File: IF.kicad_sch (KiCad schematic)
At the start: 34 parts, among them J1 JACK_TRS_3pins, U16 NE5532

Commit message: schematics mixer progress, 74HC4053, IF RX. PCB update
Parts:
- removed C16, C17: 220pF, LCSDR:C_Disc_D7.5mm_W2.5mm_P5.00mm, symbol C_Small
- removed C18, C6: 100nF, LCSDR:C_1206_0603, symbol C_Small
- removed C19, C33, C45: 10uF, LCSDR:CP_Radial_D5.0mm_P2.00mm, symbol CP_Small
- removed C25, C4, C5, C8: 27nF, LCSDR:C_1206_0603, symbol C_Small
- removed C32, C35, C62, C63: 10uF, Capacitors_THT:CP_Radial_D5.0mm_P2.00mm, symbol CP_Small
- removed J1: JACK_TRS_3pins, LCSDR:audio_jack_3_5mm_PJ307, symbol JACK_TRS_3pins
- removed L3: 100uH, Resistors_THT:R_Axial_DIN0207_L6.3mm_D2.5mm_P15.24mm_Horizontal, symbol L_Small
- removed R14, R17, R24, R46: 1k, LCSDR:R_0603_HandSoldering, symbol R_Small
- removed R2, R3, R32, R33: 33R, LCSDR:R_1206_0603, symbol R_Small
- removed R47, R48, R49, R50: 22k, LCSDR:R_0603_HandSoldering, symbol R_Small
- removed R51, R62: 1k, LCSDR:R_1206_0603, symbol R_Small
- removed R63, R64: 10k, LCSDR:R_0603_HandSoldering, symbol R_Small
- removed U16: NE5532, Housings_SOIC:SOIC-8_3.9x4.9mm_Pitch1.27mm, symbol NE5532
- added K1: G5V-2_Split, Relay_THT:Relay_DPDT_Omron_G5V-2, symbol Relay:G5V-2_Split
- added R8: 3k, symbol Device:R_Small
- added U5: MC33079, symbol Amplifier_Operational:MC33079

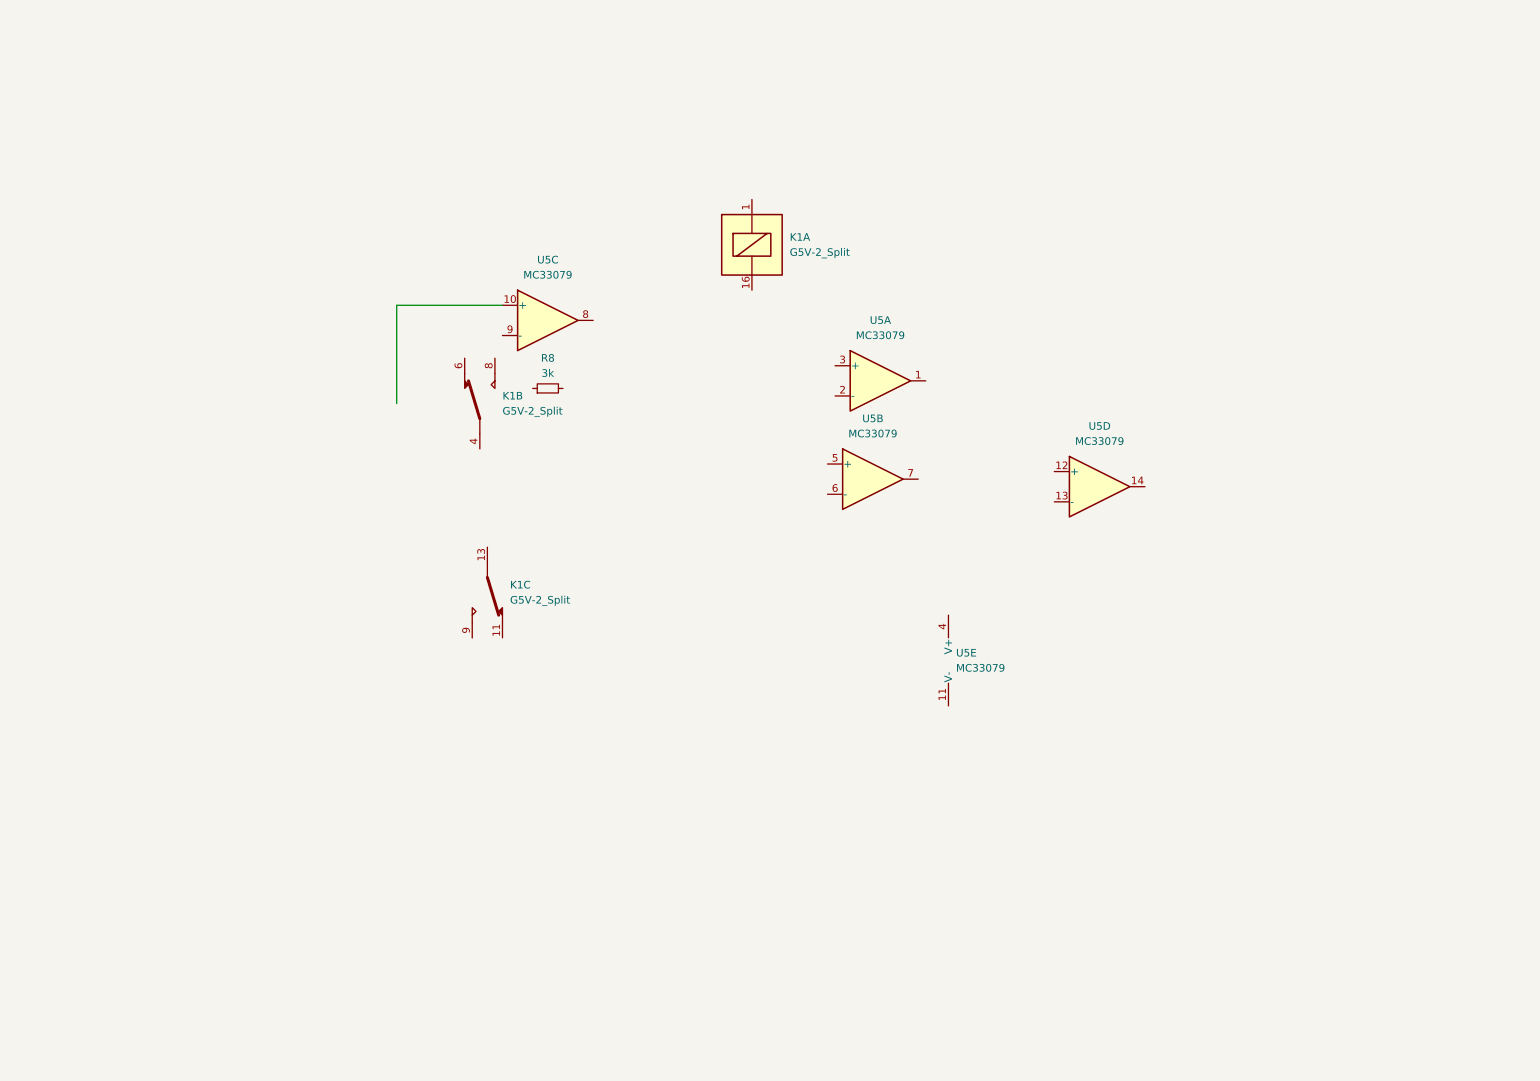
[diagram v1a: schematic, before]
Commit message: schematics mixer, 74HC4053. IF RX needs JLCPCB numbers. PCB update
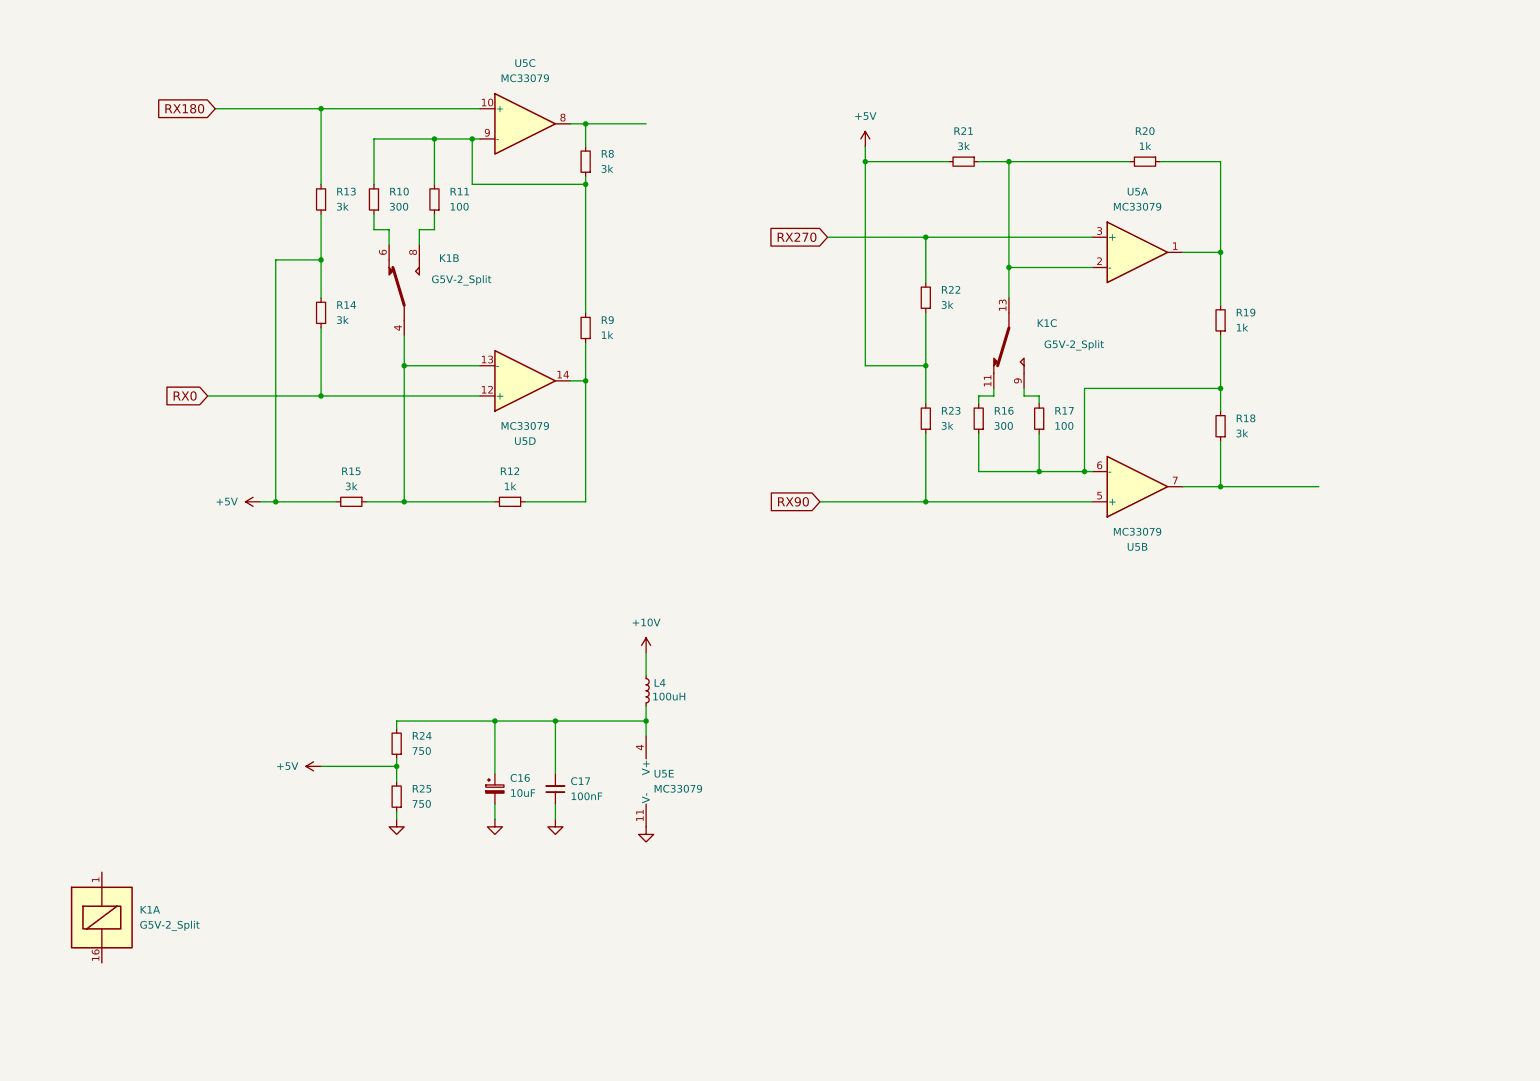
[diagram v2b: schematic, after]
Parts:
- added C16: 10uF, Capacitor_Tantalum_SMD:CP_EIA-3216-18_Kemet-A_Pad1.58x1.35mm_HandSolder, symbol Device:C_Polarized_Small
- added C17: 100nF, Capacitor_SMD:C_0603_1608Metric_Pad1.08x0.95mm_HandSolder, symbol Device:C_Small
- added L4: 100uH, Inductor_SMD:L_1210_3225Metric_Pad1.42x2.65mm_HandSolder, symbol Device:L_Small
- added R10, R16: 300, Resistor_SMD:R_0603_1608Metric_Pad0.98x0.95mm_HandSolder, symbol Device:R_Small
- added R11, R17: 100, Resistor_SMD:R_0603_1608Metric_Pad0.98x0.95mm_HandSolder, symbol Device:R_Small
- added R12, R19, R20, R9: 1k, Resistor_SMD:R_0603_1608Metric_Pad0.98x0.95mm_HandSolder, symbol Device:R_Small
- added R13, R14, R15, R18, R21, R22, R23: 3k, Resistor_SMD:R_0603_1608Metric_Pad0.98x0.95mm_HandSolder, symbol Device:R_Small
- added R24, R25: 750, Resistor_SMD:R_0603_1608Metric_Pad0.98x0.95mm_HandSolder, symbol Device:R_Small
- R8: footprint (none) -> Resistor_SMD:R_0603_1608Metric_Pad0.98x0.95mm_HandSolder
- U5: footprint (none) -> Package_SO:SOIC-14_3.9x8.7mm_P1.27mm
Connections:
- net RX180: now reaches U5.10 (+)
- net RX180: now also R13.2
- net at U5.8: now also R8.2
- net at U5.9 (-): now also R8.1, R10.2, R11.2, R9.2
- net at K1.4: now also U5.13 (-), R12.2, R15.1
- net at K1.6: now also R10.1
- net at K1.8: now also R11.1
- net GND: now reaches U5.11 (V-)
- net GND: now also C16.2, C17.1, R25.1
- net at U5.4 (V+): now also C16.1, C17.2, L4.2, R24.2
- net at K1.11: now also R16.2
- net at K1.13: now also U5.2 (-), R20.2, R21.1
- net at K1.9: now also R17.2
- net RX90: now reaches U5.5 (+)
- net RX90: now also R23.1
- net at U5.6 (-): now also R16.1, R17.1, R18.2, R19.1
- net at U5.7: now also R18.1
- net at U5.1: now also R19.2, R20.1
- net RX270: now reaches U5.3 (+)
- net RX270: now also R22.2
- net RX0: now reaches U5.12 (+)
- net RX0: now also R14.1
- net at U5.14: now also R12.1, R9.1
- new net +10V: L4.1
- new net +5V: R13.1, R14.2, R15.2, R21.2, R22.1, R23.2, R24.1, R25.2
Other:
- moved on the sheet: K1A, K1B, K1C, R8, U5A, U5B, U5C, U5D, U5E

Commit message: some minor changes, IF RX, 74HC4053, page numbers
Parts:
- R12, R19, R20, R9: JLCPCB (none) -> C21190
- R13, R14, R15, R18, R21, R22, R23, R8: JLCPCB (none) -> C4211
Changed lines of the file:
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@@
+			)
+		)
+		(property "JLCPCB" "C4211"
+			(at 77.47 66.04 0)
+			(effects
+				(font
+					(size 1.524 1.524)
+				)
+				(hide yes)
 			)
 		)
@@
 			)
 		)
+		(property "JLCPCB" "C4211"
+			(at 185.42 40.64 90)
+			(effects
+				(font
+					(size 1.524 1.524)
+				)
+				(hide yes)
+			)
+		)
 		(pin "1"
 		)
@@
 			)
 		)
+		(property "JLCPCB" "C4211"
+			(at 82.55 97.79 90)
+			(effects
+				(font
+					(size 1.524 1.524)
+				)
+				(hide yes)
+			)
+		)
 		(pin "1"
 		)
@@
 			)
 		)
+		(property "JLCPCB" "C4211"
+			(at 179.07 83.82 0)
+			(effects
+				(font
+					(size 1.524 1.524)
+				)
+				(hide yes)
+			)
+		)
 		(pin "1"
 		)
@@
 				(font
 					(size 1.27 1.27)
+				)
+				(hide yes)
+			)
+		)
+		(property "JLCPCB" "C4211"
+			(at 121.92 40.64 0)
+			(effects
+				(font
+					(size 1.524 1.524)
 				)
 				(hide yes)
@@
 			)
 		)
+		(property "JLCPCB" "C21190"
+			(at 228.6 67.31 0)
+			(effects
+				(font
+					(size 1.524 1.524)
+				)
+				(hide yes)
+			)
+		)
 		(pin "1"
 		)
@@
 			)
 		)
+		(property "JLCPCB" "C21190"
+			(at 109.22 97.79 90)
+			(effects
+				(font
+					(size 1.524 1.524)
+				)
+				(hide yes)
+			)
+		)
 		(pin "1"
 		)
@@
 			)
 		)
+		(property "JLCPCB" "C4211"
+			(at 77.47 46.99 0)
+			(effects
+				(font
+					(size 1.524 1.524)
+				)
+				(hide yes)
+			)
+		)
 		(pin "1"
 		)
@@
 			)
 		)
+		(property "JLCPCB" "C4211"
+			(at 228.6 85.09 0)
+			(effects
+				(font
+					(size 1.524 1.524)
+				)
+				(hide yes)
+			)
+		)
 		(pin "1"
 		)
@@
 			)
 		)
+		(property "JLCPCB" "C21190"
+			(at 121.92 68.58 0)
+			(effects
+				(font
+					(size 1.524 1.524)
+				)
+				(hide yes)
+			)
+		)
 		(pin "1"
 		)
@@
 				(font
 					(size 1.27 1.27)
+				)
+				(hide yes)
+			)
+		)
+		(property "JLCPCB" "C4211"
+			(at 179.07 63.5 0)
+			(effects
+				(font
+					(size 1.524 1.524)
 				)
 				(hide yes)
@@
 				)
 				(hide yes)
+			)
+		)
+		(property "JLCPCB" "C21190"
+			(at 215.9 40.64 90)
+			(effects
+				(font
+					(size 1.524 1.524)
+				)
+				(hide yes)

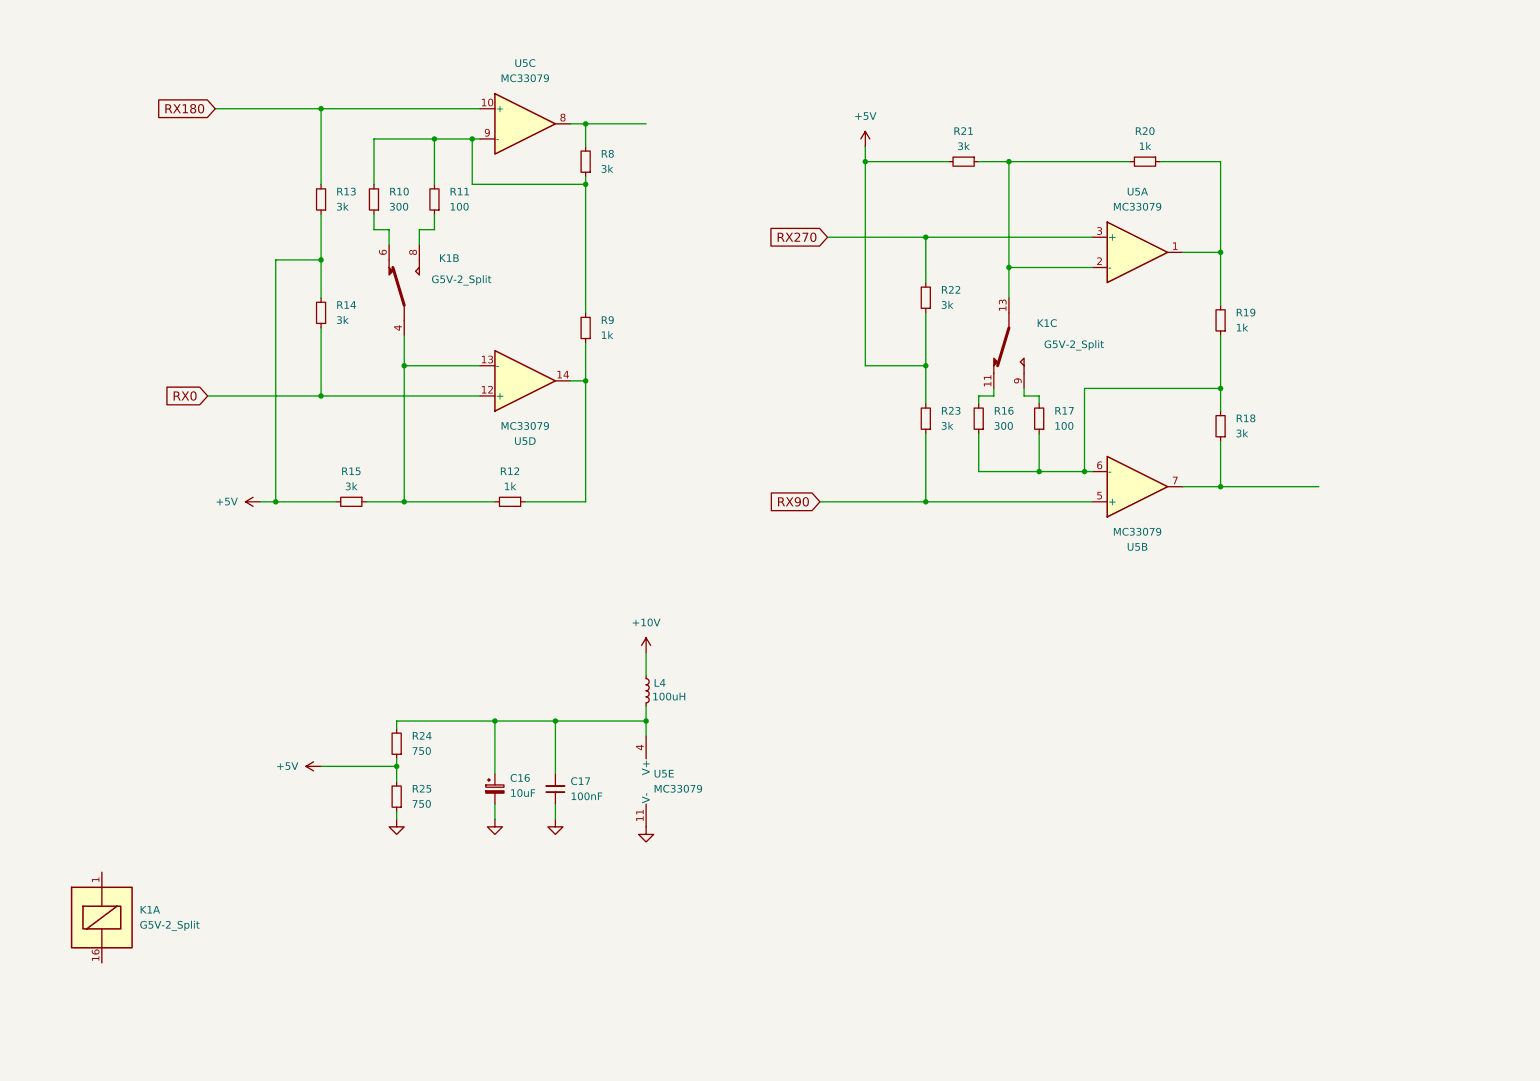
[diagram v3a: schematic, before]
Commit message: finich IF_RX_Schematics, begin MCU, delete *.sch files
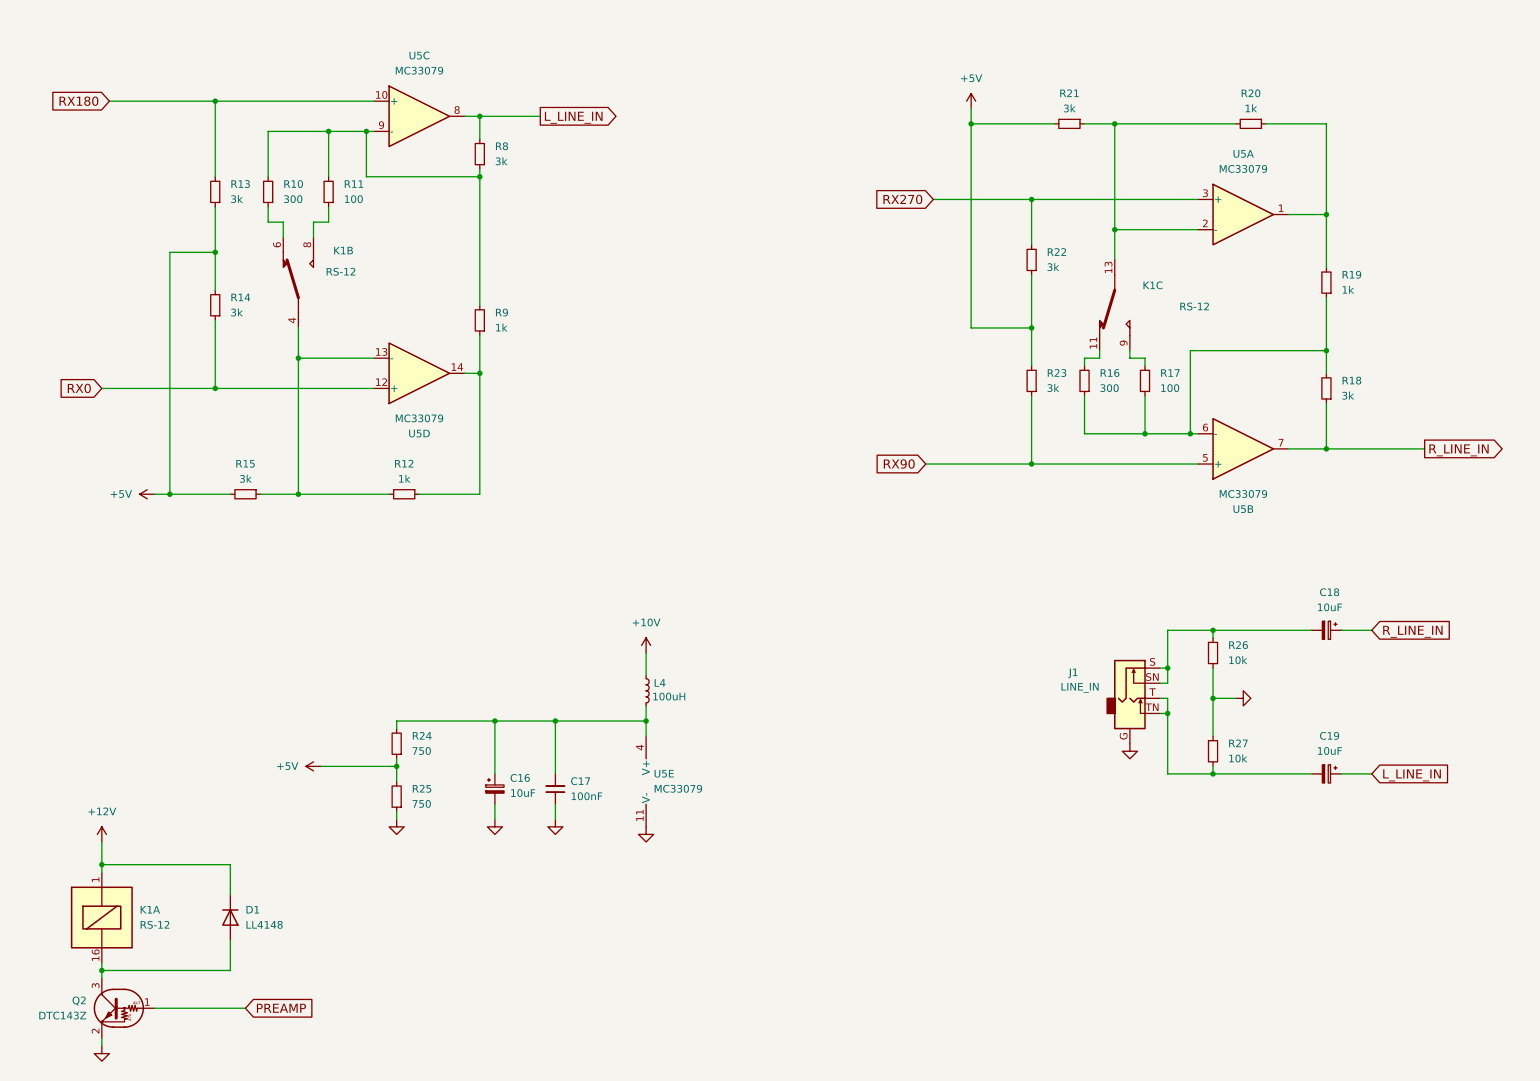
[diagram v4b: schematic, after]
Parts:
- added C18, C19: 10uF, Capacitor_Tantalum_SMD:CP_EIA-3216-18_Kemet-A_Pad1.58x1.35mm_HandSolder, symbol Device:C_Polarized_Small
- added D1: LL4148, Diode_SMD:D_MiniMELF, symbol Diode:LL4148
- added J1: LINE_IN, Connector_Audio:Jack_3.5mm_CUI_SJ1-3525N_Horizontal, symbol Connector_Audio:AudioJack2_Ground_Switch
- added Q2: DTC143Z, Package_TO_SOT_SMD:SOT-523, symbol Transistor_BJT:DTC143Z
- added R26, R27: 10k, Resistor_SMD:R_0603_1608Metric_Pad0.98x0.95mm_HandSolder, symbol Device:R_Small
- K1: value G5V-2_Split -> RS-12
- R10, R16: JLCPCB (none) -> C23025
- R11, R17: JLCPCB (none) -> C22775
- R24, R25: JLCPCB (none) -> C23241
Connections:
- net GND: now also J1.G, Q2.2 (E), R26.2, R27.1
- net L_LINE_IN: now reaches R8.2, U5.8
- net L_LINE_IN: now also C19.1
- net +12V: now reaches K1.1
- net +12V: now also D1.1 (K)
- net at K1.16: now also D1.2 (A), Q2.3 (C)
- net R_LINE_IN: now reaches R18.1, U5.7
- net R_LINE_IN: now also C18.1
- new net: C19.2, J1.T, J1.TN, R27.2
- new net: C18.2, J1.S, J1.SN, R26.1
- new net PREAMP: Q2.1 (B)
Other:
- moved on the sheet: K1B, K1C, R10, R11, R12, R13, R14, R15, R16, R17, R18, R19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
